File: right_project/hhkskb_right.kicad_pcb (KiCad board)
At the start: 2 copper layers, 168 x 118 mm, 92 parts, among them J1 4pin_Jack, SW11 SW_PUSH, SW12 SW_PUSH, SW13 SW_PUSH, SW14 SW_PUSH, SW15 SW_PUSH, SW16 SW_PUSH, SW17 SW_PUSH, SW21 SW_PUSH, SW22 SW_PUSH, SW23 SW_PUSH, SW24 SW_PUSH, SW25 SW_PUSH, SW26 SW_PUSH, SW27 SW_PUSH, SW28 SW_PUSH, SW31 SW_PUSH, SW32 SW_PUSH, SW33 SW_PUSH, SW34 SW_PUSH, SW35 SW_PUSH, SW36 SW_PUSH, SW37 SW_PUSH, SW41 SW_PUSH, SW42 SW_PUSH, SW43 SW_PUSH, SW44 SW_PUSH, SW45 SW_PUSH, SW46 SW_PUSH, SW47 SW_PUSH, SW48 SW_PUSH, SW51 SW_PUSH, SW52 SW_PUSH, SW53 SW_PUSH, SW54 SW_PUSH, SW55 SW_PUSH, SW56 SW_PUSH, SW57 SW_PUSH, U1 ARDUINO_MICRO_SHIELD

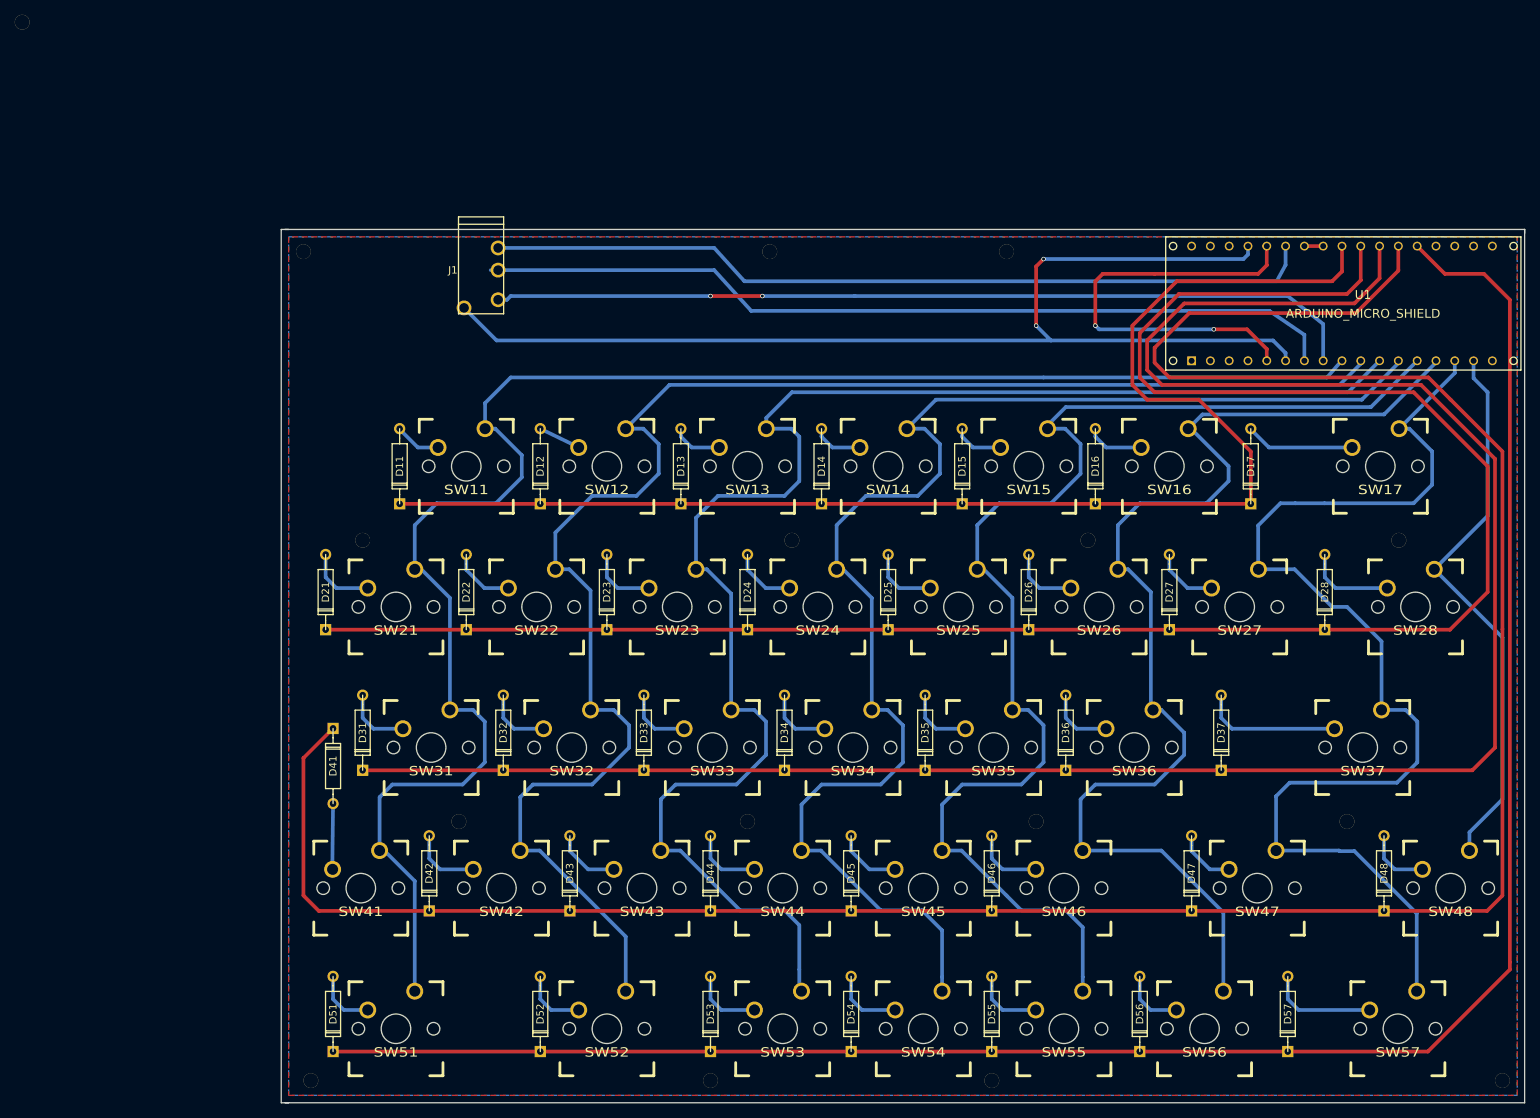
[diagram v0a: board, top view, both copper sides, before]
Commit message: キーレイアウト変更 *  一行目7キーを2つに分離 ** バックスラッシュとにょろで使う。 ** 二行目8キーはDeleteに変更 M2ねじのホール定義を変更 * 穴を2.5に変更 * ランドをねじ頭分3.5用意 ねじ穴を大量に用意
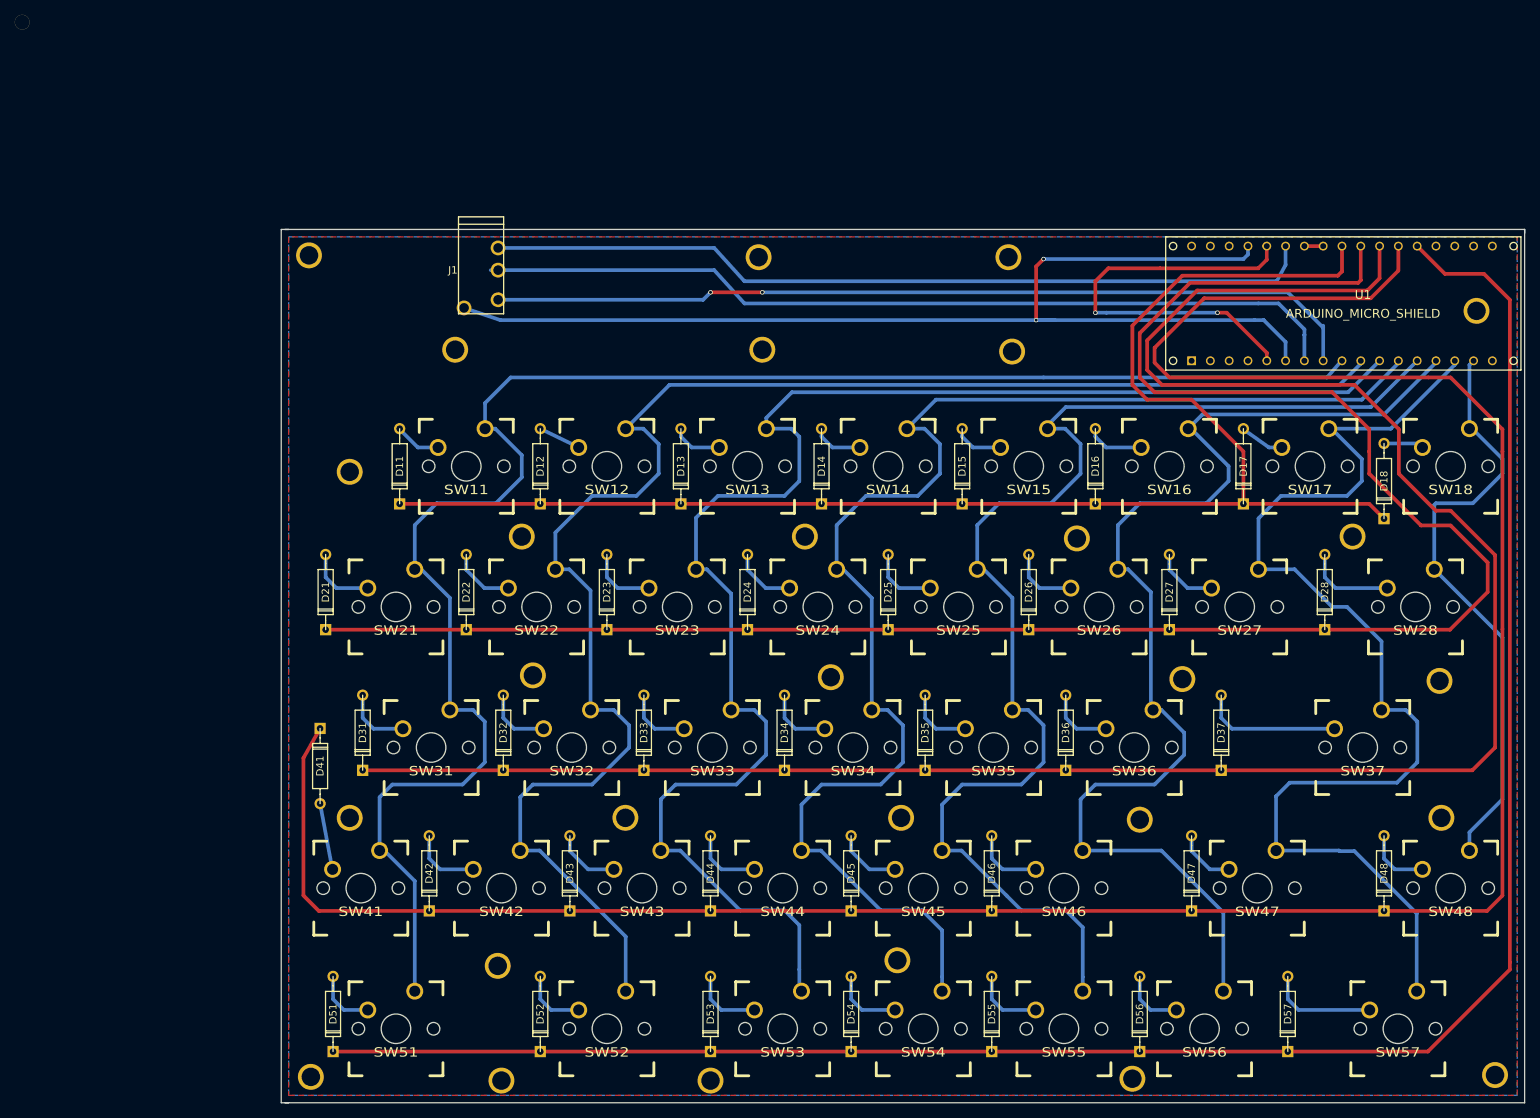
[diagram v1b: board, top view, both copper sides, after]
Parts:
- removed the ? at (186.0, 70.0)
- removed the ? at (46.0, 70.0)
- removed the ? at (104.0, 70.0)
- removed the ? at (144.0, 70.0)
- removed the ? at (133.0, 31.0)
- removed the ? at (38.0, 31.0)
- removed the ? at (101.0, 31.0)
- removed the ? at (39.0, 143.0)
- removed the ? at (93.0, 143.0)
- removed the ? at (131.0, 143.0)
- removed the ? at (200.0, 143.0)
- removed the ? at (59.0, 108.0)
- removed the ? at (98.0, 108.0)
- removed the ? at (137.0, 108.0)
- removed the ? at (179.0, 108.0)
- added ?: , MyFootprint:m2_neji_hole2.5_head3.5, F.Cu at (81.5, 107.5)
- added ?: , MyFootprint:m2_neji_hole2.5_head3.5, F.Cu at (118.8, 107.5)
- added ?: , MyFootprint:m2_neji_hole2.5_head3.5, F.Cu at (151.0, 107.8)
- added ?: , MyFootprint:m2_neji_hole2.5_head3.5, F.Cu at (191.8, 107.5)
- added ?: , MyFootprint:m2_neji_hole2.5_head3.5, F.Cu at (179.8, 69.5)
- added ?: , MyFootprint:m2_neji_hole2.5_head3.5, F.Cu at (142.5, 69.8)
- added ?: , MyFootprint:m2_neji_hole2.5_head3.5, F.Cu at (105.8, 69.5)
- added ?: , MyFootprint:m2_neji_hole2.5_head3.5, F.Cu at (67.5, 69.5)
- added ?: , MyFootprint:m2_neji_hole2.5_head3.5, F.Cu at (44.2, 60.8)
- added ?: , MyFootprint:m2_neji_hole2.5_head3.5, F.Cu at (196.5, 39.0)
- added ?: , MyFootprint:m2_neji_hole2.5_head3.5, F.Cu at (199.0, 142.2)
- added ?: , MyFootprint:m2_neji_hole2.5_head3.5, F.Cu at (64.8, 143.0)
- added ?: , MyFootprint:m2_neji_hole2.5_head3.5, F.Cu at (133.8, 44.5)
- added ?: , MyFootprint:m2_neji_hole2.5_head3.5, F.Cu at (100.0, 44.2)
- added ?: , MyFootprint:m2_neji_hole2.5_head3.5, F.Cu at (58.5, 44.2)
- added ?: , MyFootprint:m2_neji_hole2.5_head3.5, F.Cu at (191.5, 89.0)
- added ?: , MyFootprint:m2_neji_hole2.5_head3.5, F.Cu at (156.8, 88.8)
- added ?: , MyFootprint:m2_neji_hole2.5_head3.5, F.Cu at (109.2, 88.5)
- added ?: , MyFootprint:m2_neji_hole2.5_head3.5, F.Cu at (69.0, 88.2)
- added ?: , MyFootprint:m2_neji_hole2.5_head3.5, F.Cu at (64.2, 127.5)
- added ?: , MyFootprint:m2_neji_hole2.5_head3.5, F.Cu at (118.2, 126.8)
- added ?: , MyFootprint:m2_neji_hole2.5_head3.5, F.Cu at (39.0, 142.5)
- added ?: , MyFootprint:m2_neji_hole2.5_head3.5, F.Cu at (150.0, 142.8)
- added ?: , MyFootprint:m2_neji_hole2.5_head3.5, F.Cu at (93.0, 143.0)
- added ?: , MyFootprint:m2_neji_hole2.5_head3.5, F.Cu at (133.2, 31.8)
- added ?: , MyFootprint:m2_neji_hole2.5_head3.5, F.Cu at (99.5, 31.8)
- added ?: , MyFootprint:m2_neji_hole2.5_head3.5, F.Cu at (38.8, 31.5)
- added ?: , MyFootprint:m2_neji_hole2.5_head3.5, F.Cu at (44.2, 107.5)
- added D18: D, Discret:DO-41, F.Cu at (184.0, 62.0)
- added SW18: SW_PUSH, MyFootprint:CHERRY_PLATE_100H, F.Cu at (193.0, 60.0)
- SW17: footprint MyFootprint:CHERRY_PLATE_200H -> MyFootprint:CHERRY_PLATE_100H
- moved SW17 9.50 mm to (174.0, 60.0)
- moved D41 1.75 mm to (40.2, 100.5)
- moved D17 1.00 mm to (165.0, 60.0)
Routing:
- net /INPUT1: track 184.7 -> 202.5 mm
- net Net-(D17-Pad2): track 14.8 -> 6.11 mm
- net Net-(D18-Pad2): track 0.00 -> 5.41 mm
- net /OUTPUT8: track 76.2 -> 81.5 mm
- net /INPUT3: track 288.5 -> 284.4 mm
- net /INPUT2: track 271.9 -> 267.8 mm
- net Net-(U1-PadRST): track 59.1 -> 57.4 mm
- net /OUTPUT7: track 156.5 -> 155.5 mm
- net /SDA: track 116.9 -> 117.6 mm
- net /SCL: track 118.0 -> 118.7 mm
- net /INPUT4: track 342.5 -> 343.2 mm
- net GND: track 155.8 -> 155.2 mm

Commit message: 4pinジャックのフットプリントを修正 ドリルの位置を微調整（明らかな直線は数字を合わせた）
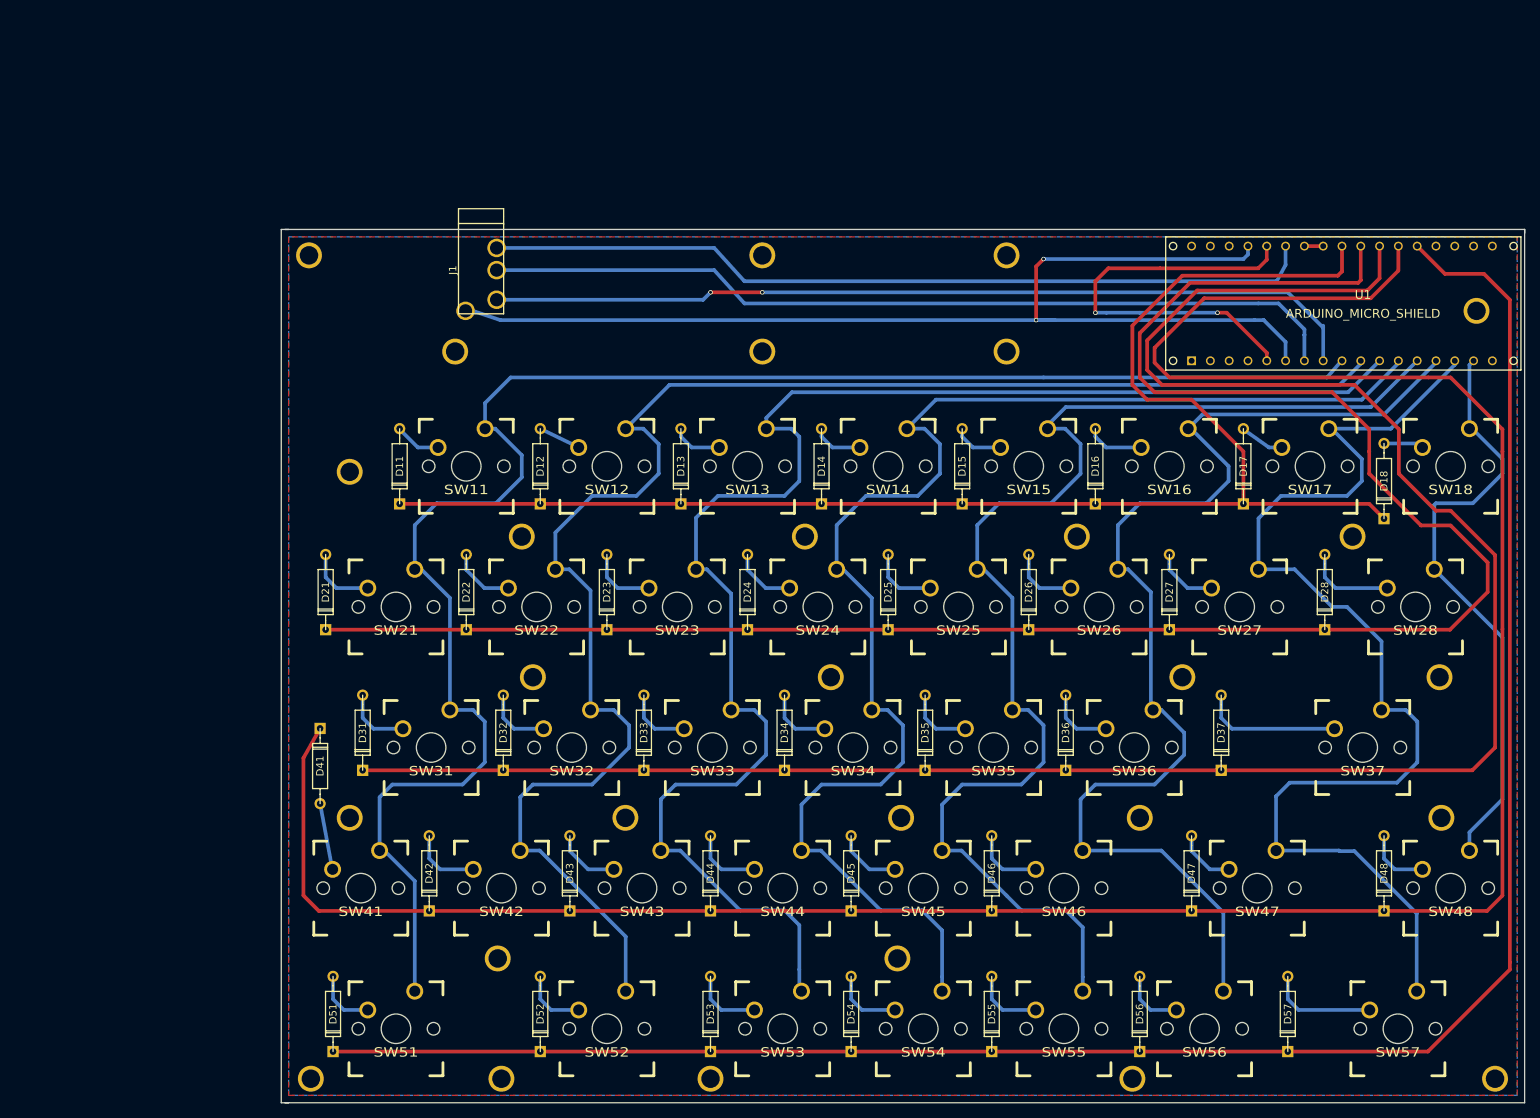
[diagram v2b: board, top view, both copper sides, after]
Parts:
- removed the ? at (0.00, 0.00)
